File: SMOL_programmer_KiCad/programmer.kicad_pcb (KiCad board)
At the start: 2 copper layers, 17.8 x 54 mm, 11 parts, among them J1 Conn_01x03_Male, J2 Conn_01x05

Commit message: Another variant programmer to test: this one's a sandwich
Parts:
- removed 2kΩ (x4): 2k, Resistors_THT:R_Axial_DIN0204_L3.6mm_D1.6mm_P5.08mm_Horizontal
- removed A1: Arduino_Nano_v3.x, Modules:Arduino_Nano
- removed the REF** at (33.7, 18.4)
- removed the REF** at (34.5, 63.5)
- removed the REF** at (21.3, 63.5)
- removed the REF** at (22.2, 18.4)
- added ?: Conn_02x03_Odd_Even, Pin_Headers:Pin_Header_Straight_2x03_Pitch2.54mm, F.Cu at (129.5, 120.0)
- added CLK: 2k, Resistors_SMD:R_0603_HandSoldering, F.Cu at (135.5, 116.3)
- added GND: Jumper_NO_Small, Resistors_SMD:R_0603_HandSoldering, F.Cu at (135.5, 118.9)
- added MISO: 2k, Resistors_SMD:R_0603_HandSoldering, F.Cu at (118.5, 121.4)
- added MOSI: 2k, Resistors_SMD:R_0603_HandSoldering, F.Cu at (135.5, 121.4)
- added PWR: Jumper_NO_Small, Resistors_SMD:R_0603_HandSoldering, F.Cu at (118.5, 118.9)
- added REF**: MountingHole_3.2mm_M3, Mounting_Holes:MountingHole_3.2mm_M3, F.Cu at (145.4, 131.5)
- added REF**: MountingHole_3.2mm_M3, Mounting_Holes:MountingHole_3.2mm_M3, F.Cu at (148.6, 131.3)
- added REF**: MountingHole_3.2mm_M3, Mounting_Holes:MountingHole_3.2mm_M3, F.Cu at (151.8, 116.5)
- added REF**: MountingHole_3.2mm_M3, Mounting_Holes:MountingHole_3.2mm_M3, F.Cu at (125.3, 116.8)
- added REF**: MountingHole_3.2mm_M3, Mounting_Holes:MountingHole_3.2mm_M3, F.Cu at (128.3, 116.8)
- added REF**: MountingHole_3.2mm_M3, Mounting_Holes:MountingHole_3.2mm_M3, F.Cu at (132.1, 108.0)
- added REF**: MountingHole_3.2mm_M3, Mounting_Holes:MountingHole_3.2mm_M3, F.Cu at (124.8, 108.0)
- added RST: 2k, Resistors_SMD:R_0603_HandSoldering, F.Cu at (118.5, 116.3)
- J1: value Conn_01x03_Male -> Conn_02x03_Odd_Even; footprint Pin_Headers:Pin_Header_Straight_1x03_Pitch2.54mm -> Pin_Headers:Pin_Header_Straight_2x03_Pitch2.54mm
- J2: moved to B.Cu
- moved J2 141.5 mm to (124.5, 115.6), turned to 270 degrees
- moved J1 127.7 mm to (124.5, 134.0)
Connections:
- J1 pad 1: Net-(A1-Pad17) -> /prog_miso
- J1 pad 2: /pwr -> /prog_pwr
- J1 pad 3: Net-(A1-Pad27) -> /prog_clk
- J2 pad 4: GNDREF -> /gnd
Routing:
- net /pwr: track 38.4 -> 8.67 mm, vias 0 -> 1
- net /att_clk: track 34.6 -> 5.16 mm, vias 0 -> 1
- net Net-(A1-Pad27): track 23.7 -> 0.00 mm
- net /prog_pwr: track 0.00 -> 15.4 mm
- net GNDREF: track 31.6 -> 17.1 mm
- net /att_reset: track 18.3 -> 5.27 mm, vias 0 -> 1
- net Net-(A1-Pad17): track 12.4 -> 0.00 mm
- net /gnd: track 0.00 -> 8.67 mm, vias 0 -> 1
- net /prog_clk: track 20.6 -> 29.2 mm
- net /prog_miso: track 23.7 -> 16.1 mm
- net /prog_mosi: track 21.2 -> 14.2 mm
- net /att_data: track 28.0 -> 21.5 mm, vias 0 -> 2
- net /prog_reset: track 29.2 -> 33.9 mm
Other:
- board size 17.8 x 54 mm -> 25.4 x 26.2 mm
- board text added: "MOSI GND RST CLK"
- board text added: "PWR MISO"
- board text added: "SMOL Program- mer sandwich Revs. 6, 6b April 2019"
- board text removed: "3.3V"
- board text removed: "5V"
- board text removed: "RST PWR DAT GND CLK"

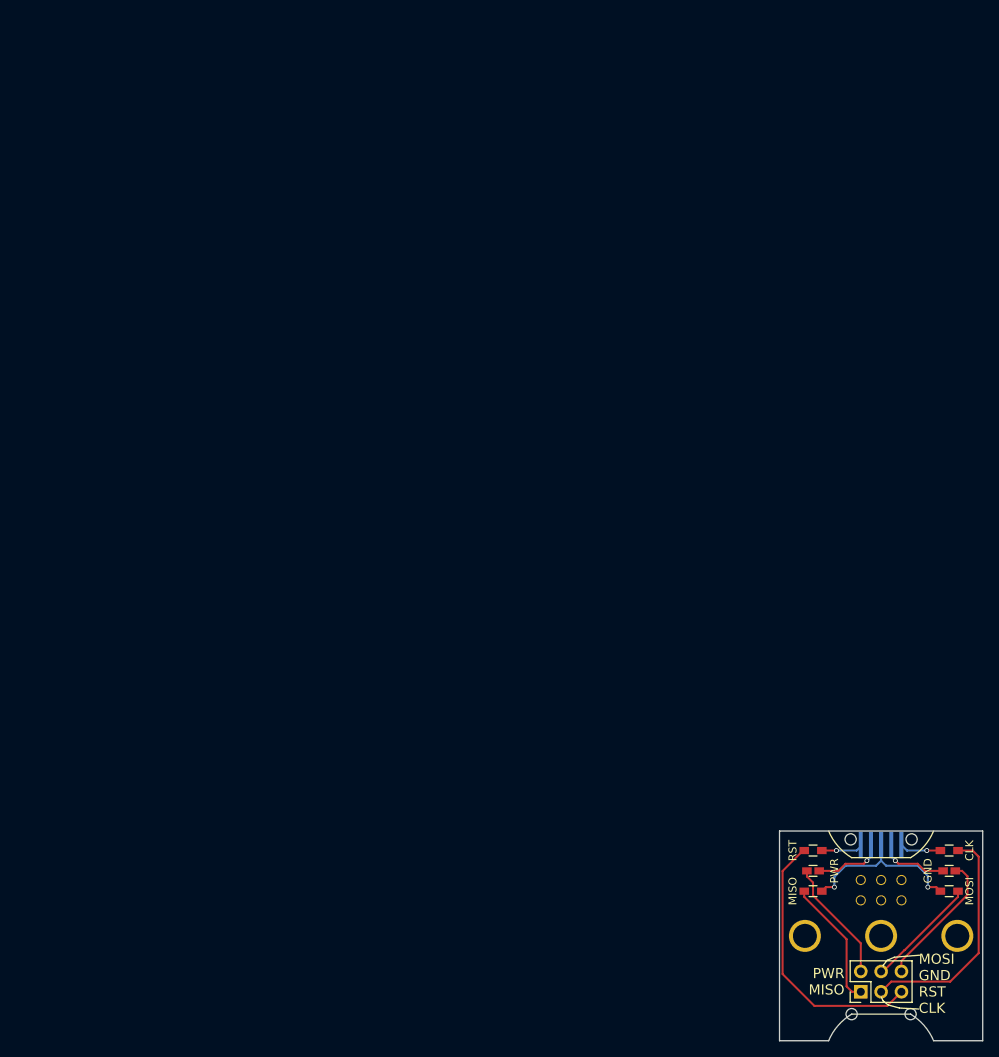
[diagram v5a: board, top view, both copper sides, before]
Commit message: Revert "Another variant programmer to test: this one's a sandwich"
This reverts commit 6c5b6402040f09fce85967fa71119872cc965c26.
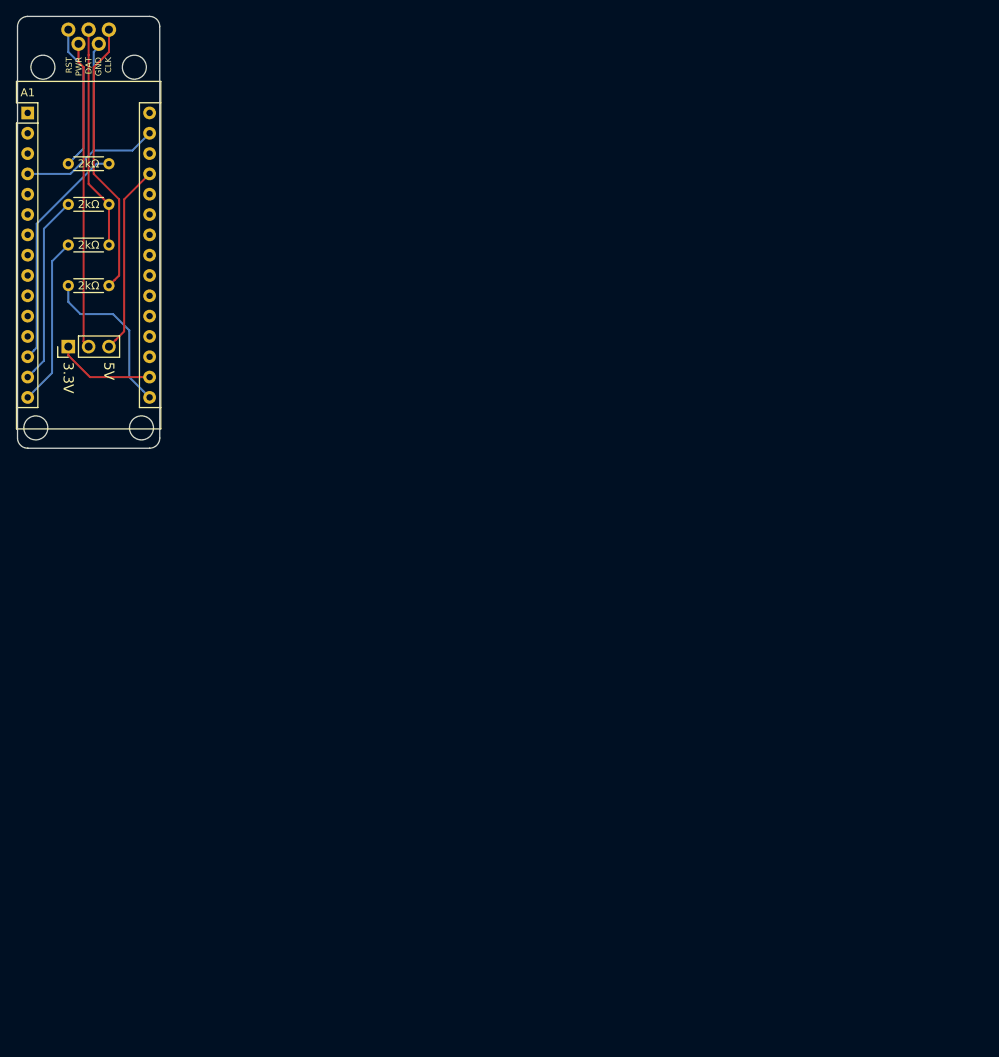
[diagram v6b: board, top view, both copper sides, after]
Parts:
- removed ?: Conn_02x03_Odd_Even, Pin_Headers:Pin_Header_Straight_2x03_Pitch2.54mm
- removed CLK, MISO, MOSI, RST: 2k, Resistors_SMD:R_0603_HandSoldering
- removed GND, PWR: Jumper_NO_Small, Resistors_SMD:R_0603_HandSoldering
- removed the REF** at (145.4, 131.5)
- removed the REF** at (148.6, 131.3)
- removed the REF** at (151.8, 116.5)
- removed the REF** at (125.3, 116.8)
- removed the REF** at (128.3, 116.8)
- removed the REF** at (132.1, 108.0)
- removed the REF** at (124.8, 108.0)
- added 2kΩ: 2k, Resistors_THT:R_Axial_DIN0204_L3.6mm_D1.6mm_P5.08mm_Horizontal, F.Cu at (30.5, 30.5)
- added 2kΩ: 2k, Resistors_THT:R_Axial_DIN0204_L3.6mm_D1.6mm_P5.08mm_Horizontal, F.Cu at (25.4, 35.6)
- added 2kΩ: 2k, Resistors_THT:R_Axial_DIN0204_L3.6mm_D1.6mm_P5.08mm_Horizontal, F.Cu at (25.4, 40.6)
- added 2kΩ: 2k, Resistors_THT:R_Axial_DIN0204_L3.6mm_D1.6mm_P5.08mm_Horizontal, F.Cu at (25.4, 45.7)
- added A1: Arduino_Nano_v3.x, Modules:Arduino_Nano, F.Cu at (20.3, 24.1)
- added REF**: MountingHole_3.2mm_M3, Mounting_Holes:MountingHole_3.2mm_M3, F.Cu at (33.7, 18.4)
- added REF**: MountingHole_3.2mm_M3, Mounting_Holes:MountingHole_3.2mm_M3, F.Cu at (34.5, 63.5)
- added REF**: MountingHole_3.2mm_M3, Mounting_Holes:MountingHole_3.2mm_M3, F.Cu at (21.3, 63.5)
- added REF**: MountingHole_3.2mm_M3, Mounting_Holes:MountingHole_3.2mm_M3, F.Cu at (22.2, 18.4)
- J1: value Conn_02x03_Odd_Even -> Conn_01x03_Male; footprint Pin_Headers:Pin_Header_Straight_2x03_Pitch2.54mm -> Pin_Headers:Pin_Header_Straight_1x03_Pitch2.54mm
- J2: moved to F.Cu
- moved J2 141.5 mm to (25.4, 14.6), turned to 90 degrees
- moved J1 127.7 mm to (25.4, 53.3)
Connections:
- J1 pad 1: /prog_miso -> Net-(A1-Pad17)
- J1 pad 2: /prog_pwr -> /pwr
- J1 pad 3: /prog_clk -> Net-(A1-Pad27)
- J2 pad 4: /gnd -> GNDREF
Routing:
- net /pwr: track 8.67 -> 38.4 mm, vias 1 -> 0
- net /att_clk: track 5.16 -> 34.6 mm, vias 1 -> 0
- net Net-(A1-Pad27): track 0.00 -> 23.7 mm
- net /prog_pwr: track 15.4 -> 0.00 mm
- net GNDREF: track 17.1 -> 31.6 mm
- net /att_reset: track 5.27 -> 18.3 mm, vias 1 -> 0
- net Net-(A1-Pad17): track 0.00 -> 12.4 mm
- net /gnd: track 8.67 -> 0.00 mm, vias 1 -> 0
- net /prog_clk: track 29.2 -> 20.6 mm
- net /prog_miso: track 16.1 -> 23.7 mm
- net /prog_mosi: track 14.2 -> 21.2 mm
- net /att_data: track 21.5 -> 28.0 mm, vias 2 -> 0
- net /prog_reset: track 33.9 -> 29.2 mm
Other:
- board size 25.4 x 26.2 mm -> 17.8 x 54 mm
- board text added: "3.3V"
- board text added: "5V"
- board text added: "RST PWR DAT GND CLK"
- board text removed: "MOSI GND RST CLK"
- board text removed: "PWR MISO"
- board text removed: "SMOL Program- mer sandwich Revs. 6, 6b April 2019"

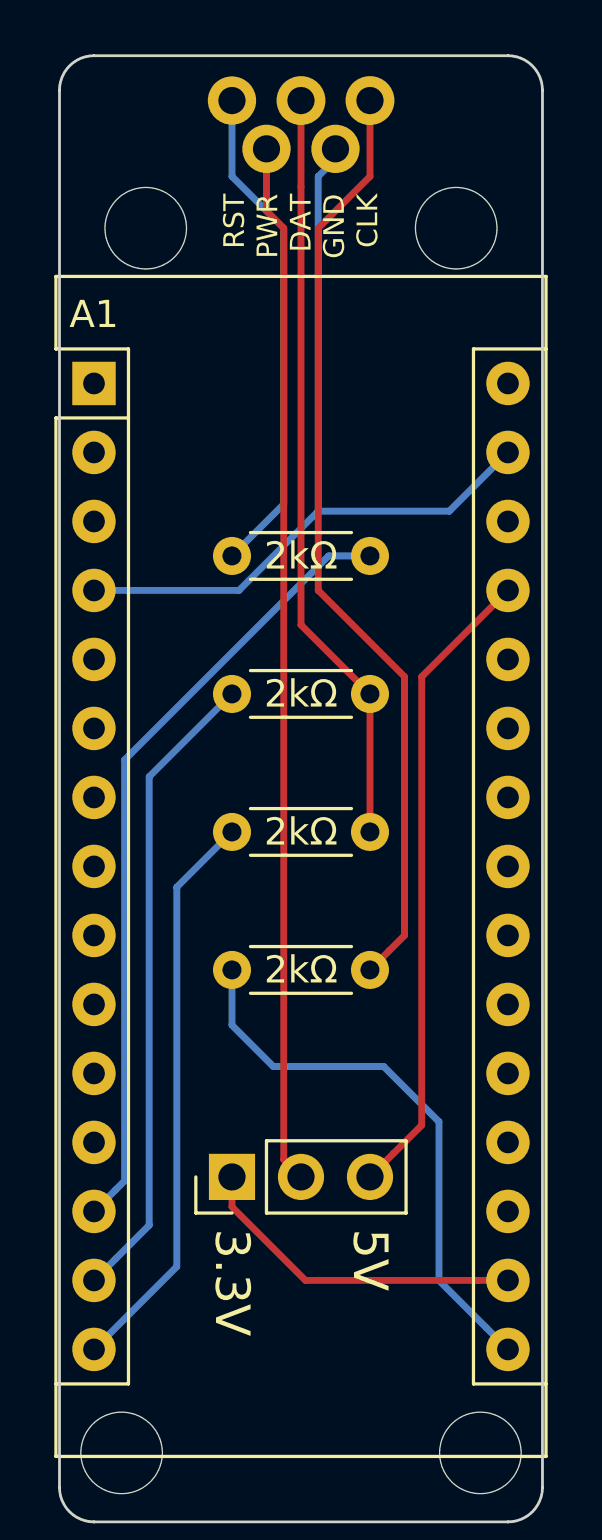
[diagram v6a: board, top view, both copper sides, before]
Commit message: Reverted the 'sandwich' programmer; tweaked the pogo-pin programmer
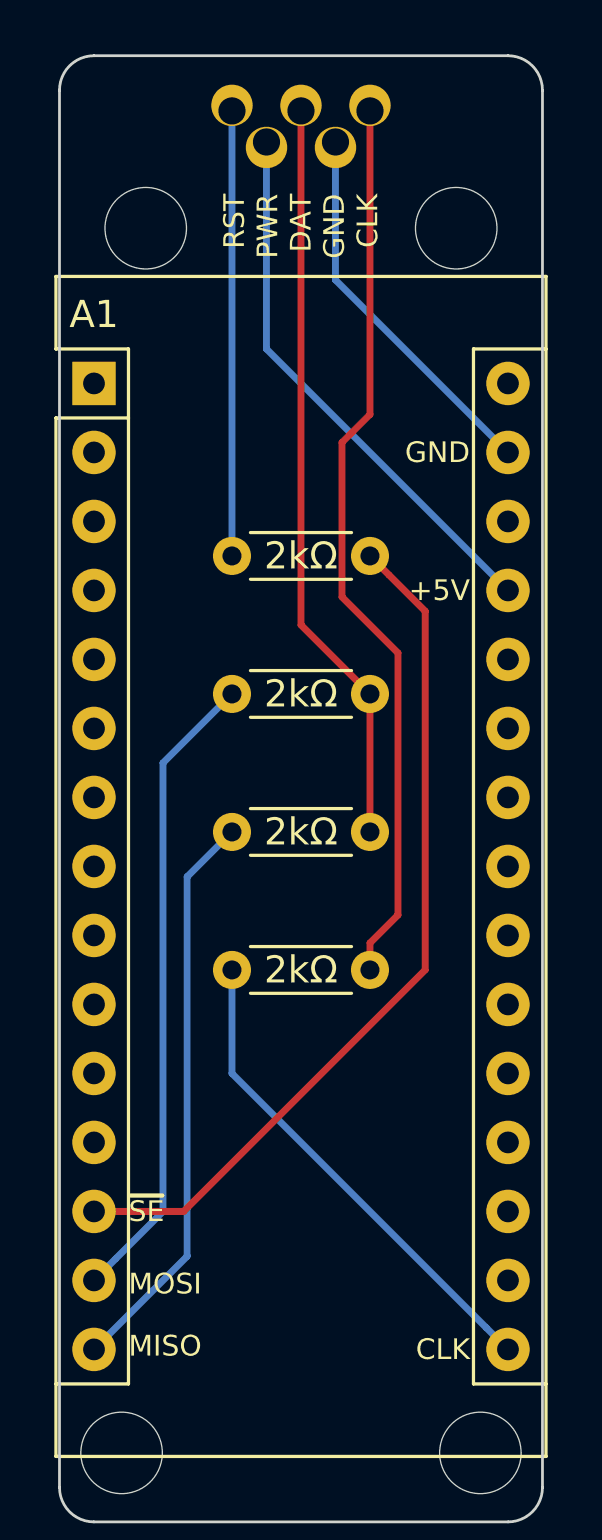
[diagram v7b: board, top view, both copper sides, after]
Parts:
- removed J1: Conn_01x03_Male, Pin_Headers:Pin_Header_Straight_1x03_Pitch2.54mm
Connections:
- A1 pad 27: Net-(A1-Pad27) -> /pwr
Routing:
- net Net-(A1-Pad27): track 23.7 -> 0.00 mm
- net /pwr: track 38.4 -> 20.2 mm
- net GNDREF: track 31.6 -> 15.1 mm
- net Net-(A1-Pad17): track 12.4 -> 0.00 mm
- net /prog_reset: track 29.2 -> 32.0 mm
- net /prog_clk: track 20.6 -> 18.2 mm
- net /att_reset: track 18.3 -> 16.4 mm
- net /att_clk: track 34.6 -> 33.3 mm
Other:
- board text added: "+5V"
- board text added: "CLK"
- board text added: "GND"
- board text added: "MISO"
- board text added: "MOSI"
- board text added: "~SE"
- board text removed: "3.3V"
- board text removed: "5V"

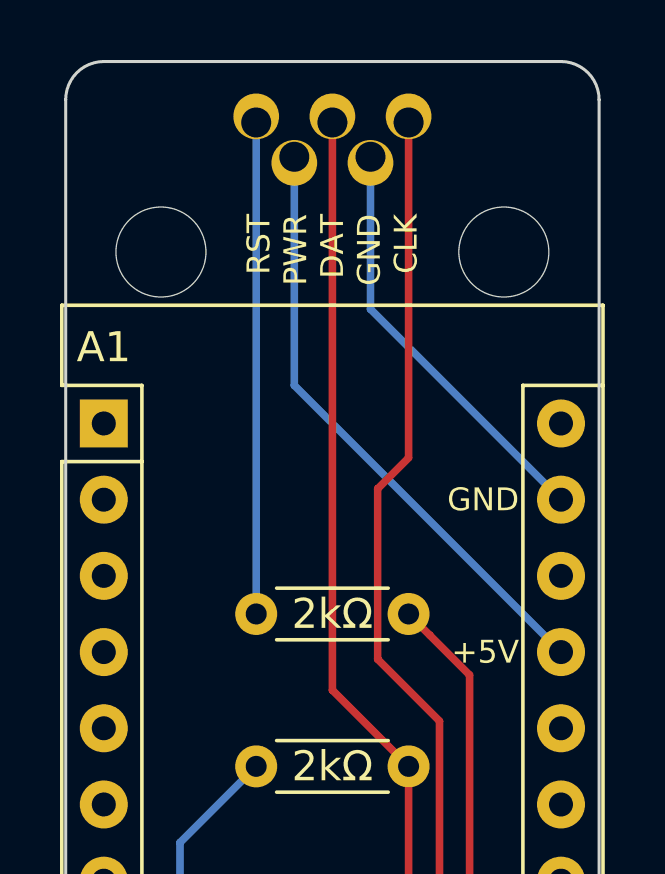
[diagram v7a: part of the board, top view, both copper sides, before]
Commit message: Revision 6c - use pogo pins for programming AND alignment
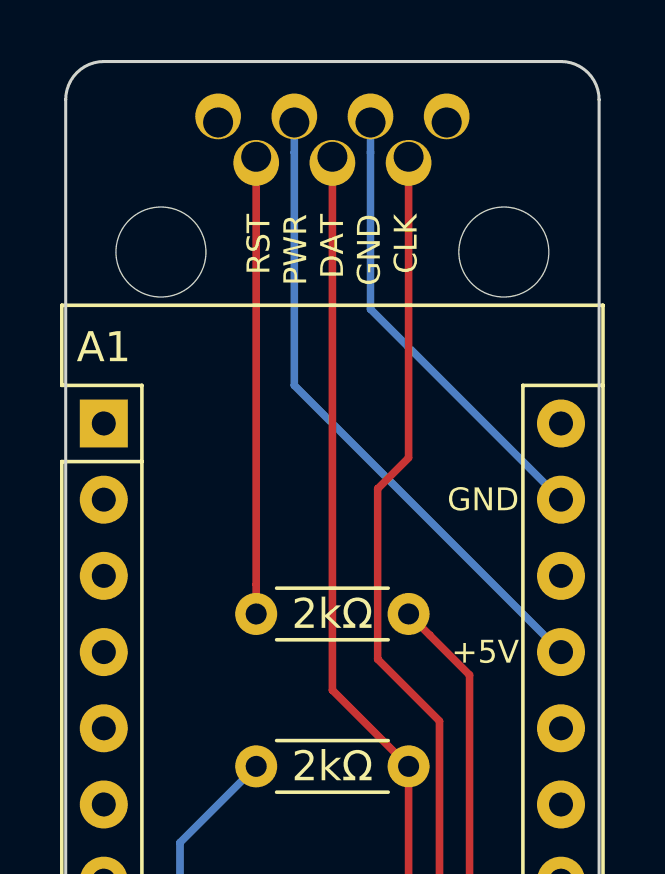
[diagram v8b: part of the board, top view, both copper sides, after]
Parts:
- added REF**: SolderWirePad_single_1mmDrill, Wire_Pads:SolderWirePad_single_1mmDrill, F.Cu at (29.8, 14.4)
- added REF**: SolderWirePad_single_1mmDrill, Wire_Pads:SolderWirePad_single_1mmDrill, F.Cu at (22.2, 14.4)
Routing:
- net /att_reset: track 16.4 -> 15.2 mm
- net /pwr: track 20.2 -> 21.3 mm
- net /att_data: track 27.6 -> 26.5 mm
- net /att_clk: track 33.3 -> 32.2 mm
- net GNDREF: track 15.1 -> 15.8 mm
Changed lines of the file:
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@@
     (thickness 1.6)
     (drawings 15)
-    (tracks 32)
+    (tracks 34)
     (zones 0)
-    (modules 10)
+    (modules 12)
     (nets 11)
   )
@@
     (uvia_drill 0.1016)
   )
+  (module Wire_Pads:SolderWirePad_single_1mmDrill (layer F.Cu)
+    (at 29.845 14.351 90)
+    (fp_text reference REF** (at 0 -3.81 90) (layer F.SilkS) hide
+      (effects (font (size 1 1) (thickness 0.15)))
+    )
+    (fp_text value SolderWirePad_single_1mmDrill (at -1.905 3.175 90) (layer F.Fab)
+      (effects (font (size 1 1) (thickness 0.15)))
+    )
+    (pad 1 thru_hole oval (at 0.254 1.905 90) (size 1.524 1.524) (drill 1 (offset 0.2032 0)) (layers *.Cu *.Mask))
+  )
   (module Mounting_Holes:MountingHole_3.2mm_M3 (layer F.Cu)
     (at 33.655 18.415)
@@
       (effects (font (size 1 1) (thickness 0.15)))
     )
-    (pad 1 thru_hole oval (at 0.508 0 90) (size 1.524 1.524) (drill 1 (offset 0.2032 0)) (layers *.Cu *.Mask)
+    (pad 1 thru_hole oval (at -0.635 0 90) (size 1.524 1.524) (drill 1 (offset -0.2032 0)) (layers *.Cu *.Mask)
       (net 6 /att_reset))
-    (pad 2 thru_hole oval (at -0.635 1.27 90) (size 1.524 1.524) (drill 1 (offset -0.2032 0)) (layers *.Cu *.Mask)
+    (pad 2 thru_hole oval (at 0.508 1.27 90) (size 1.524 1.524) (drill 1 (offset 0.2032 0)) (layers *.Cu *.Mask)
       (net 2 /pwr))
-    (pad 3 thru_hole oval (at 0.508 2.54 90) (size 1.524 1.524) (drill 1 (offset 0.2032 0)) (layers *.Cu *.Mask)
+    (pad 3 thru_hole oval (at -0.635 2.54 90) (size 1.524 1.524) (drill 1 (offset -0.2032 0)) (layers *.Cu *.Mask)
       (net 7 /att_data))
-    (pad 4 thru_hole oval (at -0.635 3.81 90) (size 1.524 1.524) (drill 1 (offset -0.2032 0)) (layers *.Cu *.Mask)
+    (pad 4 thru_hole oval (at 0.508 3.81 90) (size 1.524 1.524) (drill 1 (offset 0.2032 0)) (layers *.Cu *.Mask)
       (net 8 GNDREF))
-    (pad 5 thru_hole oval (at 0.508 5.08 90) (size 1.524 1.524) (drill 1 (offset 0.2032 0)) (layers *.Cu *.Mask)
+    (pad 5 thru_hole oval (at -0.635 5.08 90) (size 1.524 1.524) (drill 1 (offset -0.2032 0)) (layers *.Cu *.Mask)
       (net 9 /att_clk))
     (model ${KISYS3DMOD}/Pin_Headers.3dshapes/Pin_Header_Straight_1x06_Pitch2.00mm.wrl
@@
     )
   )
+  (module Wire_Pads:SolderWirePad_single_1mmDrill (layer F.Cu)
+    (at 22.225 14.351 90)
+    (fp_text reference REF** (at 0 -3.81 90) (layer F.SilkS) hide
+      (effects (font (size 1 1) (thickness 0.15)))
+    )
+    (fp_text value SolderWirePad_single_1mmDrill (at -1.905 3.175 90) (layer F.Fab)
+      (effects (font (size 1 1) (thickness 0.15)))
+    )
+    (pad 1 thru_hole oval (at 0.254 1.905 90) (size 1.524 1.524) (drill 1 (offset 0.2032 0)) (layers *.Cu *.Mask))
+  )
   (gr_text CLK (at 34.163 59.69) (layer F.SilkS)
     (effects (font (size 0.762 0.762) (thickness 0.15875)) (justify right))
@@
   (segment (start 22.86 38.1) (end 22.86 54.61) (width 0.254) (layer B.Cu) (net 1))
   (segment (start 35.56 31.75) (end 26.67 22.86) (width 0.254) (layer B.Cu) (net 2))
-  (segment (start 26.67 15.24) (end 26.67 22.86) (width 0.254) (layer B.Cu) (net 2))
+  (segment (start 26.67 15.096742) (end 26.67 14.097) (width 0.254) (layer B.Cu) (net 2))
+  (segment (start 26.67 22.86) (end 26.67 15.096742) (width 0.254) (layer B.Cu) (net 2))
   (segment (start 34.760001 58.890001) (end 35.56 59.69) (width 0.254) (layer B.Cu) (net 3))
   (segment (start 25.4 45.72) (end 25.4 49.53) (width 0.254) (layer B.Cu) (net 3))
@@
   (segment (start 20.32 54.61) (end 23.622 54.61) (width 0.254) (layer F.Cu) (net 5))
   (segment (start 23.622 54.61) (end 32.512 45.72) (width 0.254) (layer F.Cu) (net 5))
-  (segment (start 25.4 14.097) (end 25.4 30.48) (width 0.254) (layer B.Cu) (net 6))
+  (segment (start 25.4 29.490051) (end 25.4 15.24) (width 0.254) (layer F.Cu) (net 6))
+  (segment (start 25.4 30.48) (end 25.4 29.490051) (width 0.254) (layer F.Cu) (net 6))
   (segment (start 30.48 35.56) (end 30.48 40.64) (width 0.254) (layer F.Cu) (net 7))
   (segment (start 30.48 35.56) (end 27.94 33.02) (width 0.254) (layer F.Cu) (net 7))
-  (segment (start 27.94 14.097) (end 27.94 33.02) (width 0.254) (layer F.Cu) (net 7))
+  (segment (start 27.94 33.02) (end 27.94 15.24) (width 0.254) (layer F.Cu) (net 7))
   (segment (start 35.56 26.67) (end 34.925 26.67) (width 0.254) (layer B.Cu) (net 8))
-  (segment (start 29.21 15.875) (end 29.21 15.494) (width 0.254) (layer B.Cu) (net 8))
   (segment (start 35.56 26.67) (end 29.21 20.32) (width 0.254) (layer B.Cu) (net 8))
-  (segment (start 29.21 15.24) (end 29.21 20.32) (width 0.254) (layer B.Cu) (net 8))
+  (segment (start 29.21 15.096742) (end 29.21 14.097) (width 0.254) (layer B.Cu) (net 8))
+  (segment (start 29.21 20.32) (end 29.21 15.096742) (width 0.254) (layer B.Cu) (net 8))
   (segment (start 31.510201 43.69985) (end 31.510201 34.050201) (width 0.254) (layer F.Cu) (net 9))
   (segment (start 30.48 45.72) (end 30.48 44.730051) (width 0.254) (layer F.Cu) (net 9))
@@
   (segment (start 31.510201 34.050201) (end 29.449799 31.989799) (width 0.254) (layer F.Cu) (net 9))
   (segment (start 29.449799 26.303201) (end 30.48 25.273) (width 0.254) (layer F.Cu) (net 9))
-  (segment (start 30.48 25.273) (end 30.48 14.097) (width 0.254) (layer F.Cu) (net 9))
+  (segment (start 30.48 25.273) (end 30.48 15.24) (width 0.254) (layer F.Cu) (net 9))
 )
